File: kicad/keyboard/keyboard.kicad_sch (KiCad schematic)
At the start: 119 parts, among them SW1 MX_SWITCH, SW10 MX_SWITCH, SW11 MX_SWITCH, SW12 MX_SWITCH, SW13 MX_SWITCH, SW14 MX_SWITCH, SW15 MX_SWITCH, SW16 MX_SWITCH, SW17 MX_SWITCH, SW18 MX_SWITCH, SW19 MX_SWITCH, SW2 MX_SWITCH, SW20 MX_SWITCH, SW21 MX_SWITCH, SW22 MX_SWITCH, SW23 MX_SWITCH, SW24 MX_SWITCH, SW25 MX_SWITCH, SW26 MX_SWITCH, SW27 MX_SWITCH, SW28 MX_SWITCH, SW29 MX_SWITCH, SW3 MX_SWITCH, SW30 MX_SWITCH, SW31 MX_SWITCH, SW32 MX_SWITCH, SW33 MX_SWITCH, SW34 MX_SWITCH, SW35 MX_SWITCH, SW36 MX_SWITCH, SW37 MX_SWITCH, SW38 MX_SWITCH, SW39 MX_SWITCH, SW4 MX_SWITCH, SW40 MX_SWITCH, SW41 MX_SWITCH, SW42 MX_SWITCH, SW43 MX_SWITCH, SW44 MX_SWITCH, SW45 MX_SWITCH, SW46 MX_SWITCH, SW47 MX_SWITCH, SW48 MX_SWITCH, SW49 MX_SWITCH, SW5 MX_SWITCH, SW50 MX_SWITCH, SW51 MX_SWITCH, SW52 MX_SWITCH, SW53 MX_SWITCH, SW54 MX_SWITCH, SW55 MX_SWITCH, SW56 MX_SWITCH, SW57 MX_SWITCH, SW58 MX_SWITCH, SW59 MX_SWITCH, SW6 MX_SWITCH, SW7 MX_SWITCH, SW8 MX_SWITCH, SW9 MX_SWITCH

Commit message: PCB design (traces not included)
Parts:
- renumbered D56 to D45, D58 to D46, D45 to D47, D46 to D48, D47 to D49, D48 to D50, D49 to D51, D50 to D52, D51 to D53, D52 to D54, D53 to D55, D54 to D56, D55 to D57, D57 to D58, SW56 to SW45, SW58 to SW46, SW45 to SW47, SW46 to SW48, SW47 to SW49, SW48 to SW50, SW49 to SW51, SW50 to SW52, SW51 to SW53, SW52 to SW54, SW53 to SW55, SW54 to SW56, SW55 to SW57, SW57 to SW58
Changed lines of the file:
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@@
 		(dnp no)
 		(fields_autoplaced yes)
-		(property "Reference" "D47"
+		(property "Reference" "D49"
 			(at 71.12 147.3199 90)
 			(effects
@@
 			(project "keyboard"
 				(path "/61642316-f0b7-413d-bb38-e95d75ab1db2"
-					(reference "D47")
+					(reference "D49")
 					(unit 1)
 				)
@@
 		(dnp no)
 		(fields_autoplaced yes)
-		(property "Reference" "SW47"
+		(property "Reference" "SW49"
 			(at 66.04 134.62 0)
 			(effects
@@
 			(project "keyboard"
 				(path "/61642316-f0b7-413d-bb38-e95d75ab1db2"
-					(reference "SW47")
+					(reference "SW49")
 					(unit 1)
 				)
@@
 		(dnp no)
 		(fields_autoplaced yes)
-		(property "Reference" "SW53"
+		(property "Reference" "SW55"
 			(at 142.24 134.62 0)
 			(effects
@@
 			(project "keyboard"
 				(path "/61642316-f0b7-413d-bb38-e95d75ab1db2"
-					(reference "SW53")
+					(reference "SW55")
 					(unit 1)
 				)
@@
 		(dnp no)
 		(fields_autoplaced yes)
-		(property "Reference" "D48"
+		(property "Reference" "D50"
 			(at 83.82 147.3199 90)
 			(effects
@@
 			(project "keyboard"
 				(path "/61642316-f0b7-413d-bb38-e95d75ab1db2"
-					(reference "D48")
+					(reference "D50")
 					(unit 1)
 				)
@@
 		(dnp no)
 		(fields_autoplaced yes)
-		(property "Reference" "SW50"
+		(property "Reference" "SW52"
 			(at 104.14 134.62 0)
 			(effects
@@
 			(project "keyboard"
 				(path "/61642316-f0b7-413d-bb38-e95d75ab1db2"
-					(reference "SW50")
+					(reference "SW52")
 					(unit 1)
 				)
@@
 		(dnp no)
 		(fields_autoplaced yes)
-		(property "Reference" "SW45"
+		(property "Reference" "SW47"
 			(at 40.64 134.62 0)
 			(effects
@@
 			(project "keyboard"
 				(path "/61642316-f0b7-413d-bb38-e95d75ab1db2"
-					(reference "SW45")
+					(reference "SW47")
 					(unit 1)
 				)
@@
 		(dnp no)
 		(fields_autoplaced yes)
-		(property "Reference" "D52"
+		(property "Reference" "D54"
 			(at 134.62 147.3199 90)
 			(effects
@@
 			(project "keyboard"
 				(path "/61642316-f0b7-413d-bb38-e95d75ab1db2"
-					(reference "D52")
+					(reference "D54")
 					(unit 1)
 				)
@@
 		(dnp no)
 		(fields_autoplaced yes)
-		(property "Reference" "D57"
+		(property "Reference" "D58"
 			(at 185.42 147.3199 90)
 			(effects
@@
 			(project "keyboard"
 				(path "/61642316-f0b7-413d-bb38-e95d75ab1db2"
-					(reference "D57")
+					(reference "D58")
 					(unit 1)
 				)
@@
 		(dnp no)
 		(fields_autoplaced yes)
-		(property "Reference" "D46"
+		(property "Reference" "D48"
 			(at 58.42 147.3199 90)
 			(effects
@@
 			(project "keyboard"
 				(path "/61642316-f0b7-413d-bb38-e95d75ab1db2"
-					(reference "D46")
+					(reference "D48")
 					(unit 1)
 				)
@@
 		(dnp no)
 		(fields_autoplaced yes)
-		(property "Reference" "SW58"
+		(property "Reference" "SW46"
 			(at 193.04 109.22 0)
 			(effects
@@
 			(project "keyboard"
 				(path "/61642316-f0b7-413d-bb38-e95d75ab1db2"
-					(reference "SW58")
+					(reference "SW46")
 					(unit 1)
 				)
@@
 		(dnp no)
 		(fields_autoplaced yes)
-		(property "Reference" "SW49"
+		(property "Reference" "SW51"
 			(at 91.44 134.62 0)
 			(effects
@@
 			(project "keyboard"
 				(path "/61642316-f0b7-413d-bb38-e95d75ab1db2"
-					(reference "SW49")
+					(reference "SW51")
 					(unit 1)
 				)
@@
 		(dnp no)
 		(fields_autoplaced yes)
-		(property "Reference" "D54"
+		(property "Reference" "D56"
 			(at 160.02 147.3199 90)
 			(effects
@@
 			(project "keyboard"
 				(path "/61642316-f0b7-413d-bb38-e95d75ab1db2"
-					(reference "D54")
+					(reference "D56")
 					(unit 1)
 				)
@@
 		(dnp no)
 		(fields_autoplaced yes)
-		(property "Reference" "D51"
+		(property "Reference" "D53"
 			(at 121.92 147.3199 90)
 			(effects
@@
 			(project "keyboard"
 				(path "/61642316-f0b7-413d-bb38-e95d75ab1db2"
-					(reference "D51")
+					(reference "D53")
 					(unit 1)
 				)
@@
 		(dnp no)
 		(fields_autoplaced yes)
-		(property "Reference" "SW56"
+		(property "Reference" "SW45"
 			(at 180.34 109.22 0)
 			(effects
@@
 			(project "keyboard"
 				(path "/61642316-f0b7-413d-bb38-e95d75ab1db2"
-					(reference "SW56")
+					(reference "SW45")
 					(unit 1)
 				)
@@
 		(dnp no)
 		(fields_autoplaced yes)
-		(property "Reference" "D58"
+		(property "Reference" "D46"
 			(at 198.12 121.9199 90)
 			(effects
@@
 			(project "keyboard"
 				(path "/61642316-f0b7-413d-bb38-e95d75ab1db2"
-					(reference "D58")
+					(reference "D46")
 					(unit 1)
 				)
@@
 		(dnp no)
 		(fields_autoplaced yes)
-		(property "Reference" "SW46"
+		(property "Reference" "SW48"
 			(at 53.34 134.62 0)
 			(effects
@@
 			(project "keyboard"
 				(path "/61642316-f0b7-413d-bb38-e95d75ab1db2"
-					(reference "SW46")
+					(reference "SW48")
 					(unit 1)
 				)
@@
 		(dnp no)
 		(fields_autoplaced yes)
-		(property "Reference" "SW54"
+		(property "Reference" "SW56"
 			(at 154.94 134.62 0)
 			(effects
@@
 			(project "keyboard"
 				(path "/61642316-f0b7-413d-bb38-e95d75ab1db2"
-					(reference "SW54")
+					(reference "SW56")
 					(unit 1)
 				)
@@
 		(dnp no)
 		(fields_autoplaced yes)
-		(property "Reference" "D56"
+		(property "Reference" "D45"
 			(at 185.42 121.9199 90)
 			(effects
@@
 			(project "keyboard"
 				(path "/61642316-f0b7-413d-bb38-e95d75ab1db2"
-					(reference "D56")
+					(reference "D45")
 					(unit 1)
 				)
@@
 		(dnp no)
 		(fields_autoplaced yes)
-		(property "Reference" "D55"
+		(property "Reference" "D57"
 			(at 172.72 147.3199 90)
 			(effects
@@
 			(project "keyboard"
 				(path "/61642316-f0b7-413d-bb38-e95d75ab1db2"
-					(reference "D55")
+					(reference "D57")
 					(unit 1)
 				)
@@
 		(dnp no)
 		(fields_autoplaced yes)
-		(property "Reference" "SW55"
+		(property "Reference" "SW57"
 			(at 167.64 134.62 0)
 			(effects
@@
 			(project "keyboard"
 				(path "/61642316-f0b7-413d-bb38-e95d75ab1db2"
-					(reference "SW55")
+					(reference "SW57")
 					(unit 1)
 				)
@@
 		(dnp no)
 		(fields_autoplaced yes)
-		(property "Reference" "D45"
+		(property "Reference" "D47"
 			(at 45.72 147.3199 90)
 			(effects
@@
 			(project "keyboard"
 				(path "/61642316-f0b7-413d-bb38-e95d75ab1db2"
-					(reference "D45")
+					(reference "D47")
 					(unit 1)
 				)
@@
 		(dnp no)
 		(fields_autoplaced yes)
-		(property "Reference" "D49"
+		(property "Reference" "D51"
 			(at 96.52 147.3199 90)
 			(effects
@@
 			(project "keyboard"
 				(path "/61642316-f0b7-413d-bb38-e95d75ab1db2"
-					(reference "D49")
+					(reference "D51")
 					(unit 1)
 				)
@@
 		(dnp no)
 		(fields_autoplaced yes)
-		(property "Reference" "SW48"
+		(property "Reference" "SW50"
 			(at 78.74 134.62 0)
 			(effects
@@
 			(project "keyboard"
 				(path "/61642316-f0b7-413d-bb38-e95d75ab1db2"
-					(reference "SW48")
+					(reference "SW50")
 					(unit 1)
 				)
@@
 		(dnp no)
 		(fields_autoplaced yes)
-		(property "Reference" "SW57"
+		(property "Reference" "SW58"
 			(at 180.34 134.62 0)
 			(effects
@@
 			(project "keyboard"
 				(path "/61642316-f0b7-413d-bb38-e95d75ab1db2"
-					(reference "SW57")
+					(reference "SW58")
 					(unit 1)
 				)
@@
 		(dnp no)
 		(fields_autoplaced yes)
-		(property "Reference" "D50"
+		(property "Reference" "D52"
 			(at 109.22 147.3199 90)
 			(effects
@@
 			(project "keyboard"
 				(path "/61642316-f0b7-413d-bb38-e95d75ab1db2"
-					(reference "D50")
+					(reference "D52")
 					(unit 1)
 				)
@@
 		(dnp no)
 		(fields_autoplaced yes)
-		(property "Reference" "D53"
+		(property "Reference" "D55"
 			(at 147.32 147.3199 90)
 			(effects
@@
 			(project "keyboard"
 				(path "/61642316-f0b7-413d-bb38-e95d75ab1db2"
-					(reference "D53")
+					(reference "D55")
 					(unit 1)
 				)
@@
 		(dnp no)
 		(fields_autoplaced yes)
-		(property "Reference" "SW51"
+		(property "Reference" "SW53"
 			(at 116.84 134.62 0)
 			(effects
@@
 			(project "keyboard"
 				(path "/61642316-f0b7-413d-bb38-e95d75ab1db2"
-					(reference "SW51")
+					(reference "SW53")
 					(unit 1)
 				)
@@
 		(dnp no)
 		(fields_autoplaced yes)
-		(property "Reference" "SW52"
+		(property "Reference" "SW54"
 			(at 129.54 134.62 0)
 			(effects
@@
 			(project "keyboard"
 				(path "/61642316-f0b7-413d-bb38-e95d75ab1db2"
-					(reference "SW52")
+					(reference "SW54")
 					(unit 1)
 				)

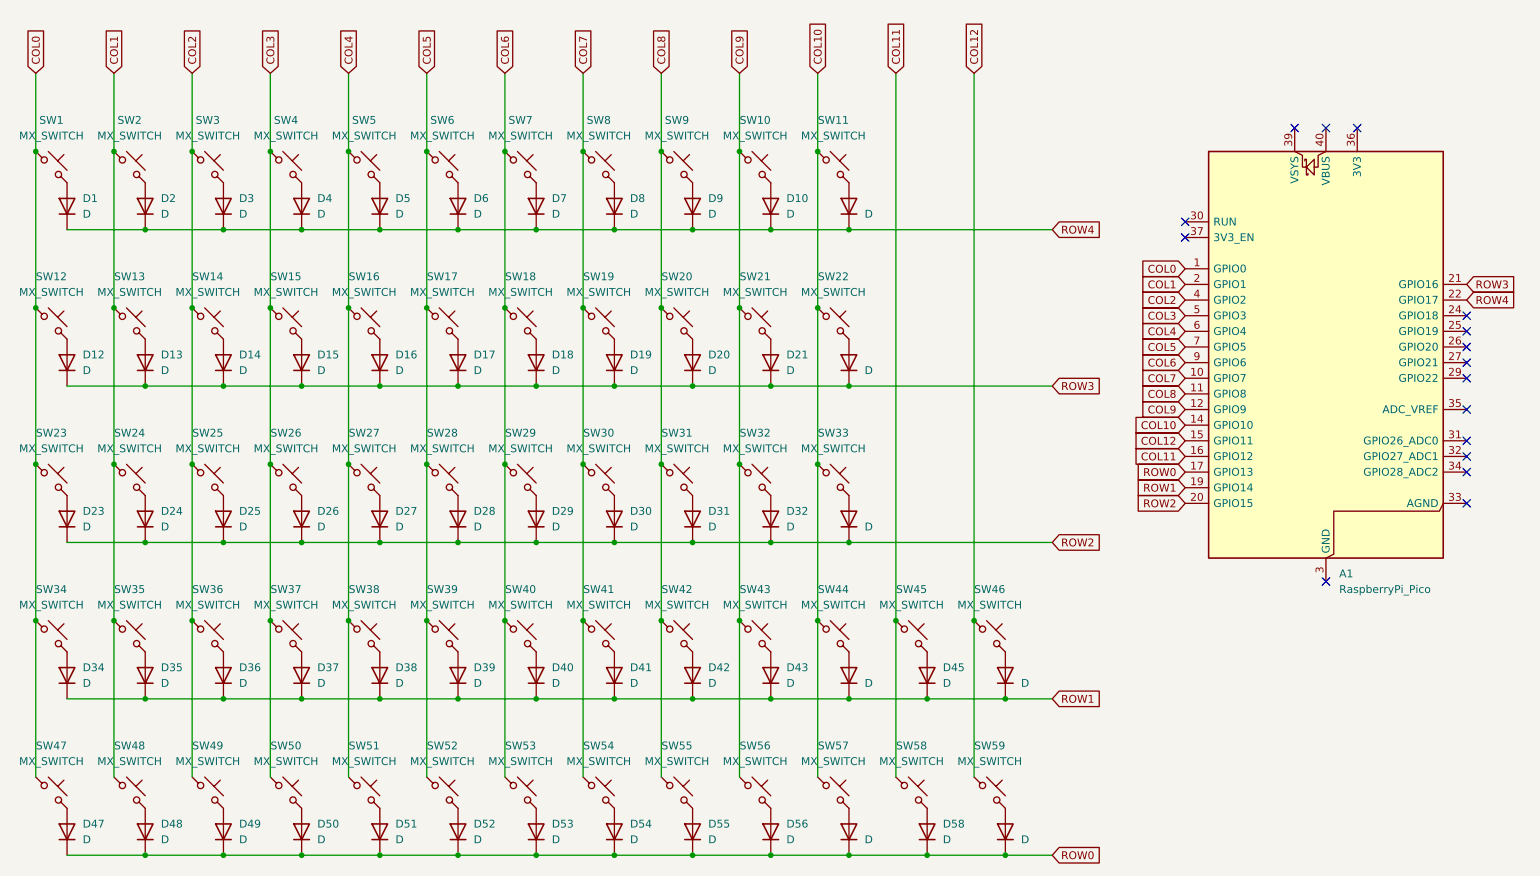
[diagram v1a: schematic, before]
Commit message: Fix incorrect switch positions
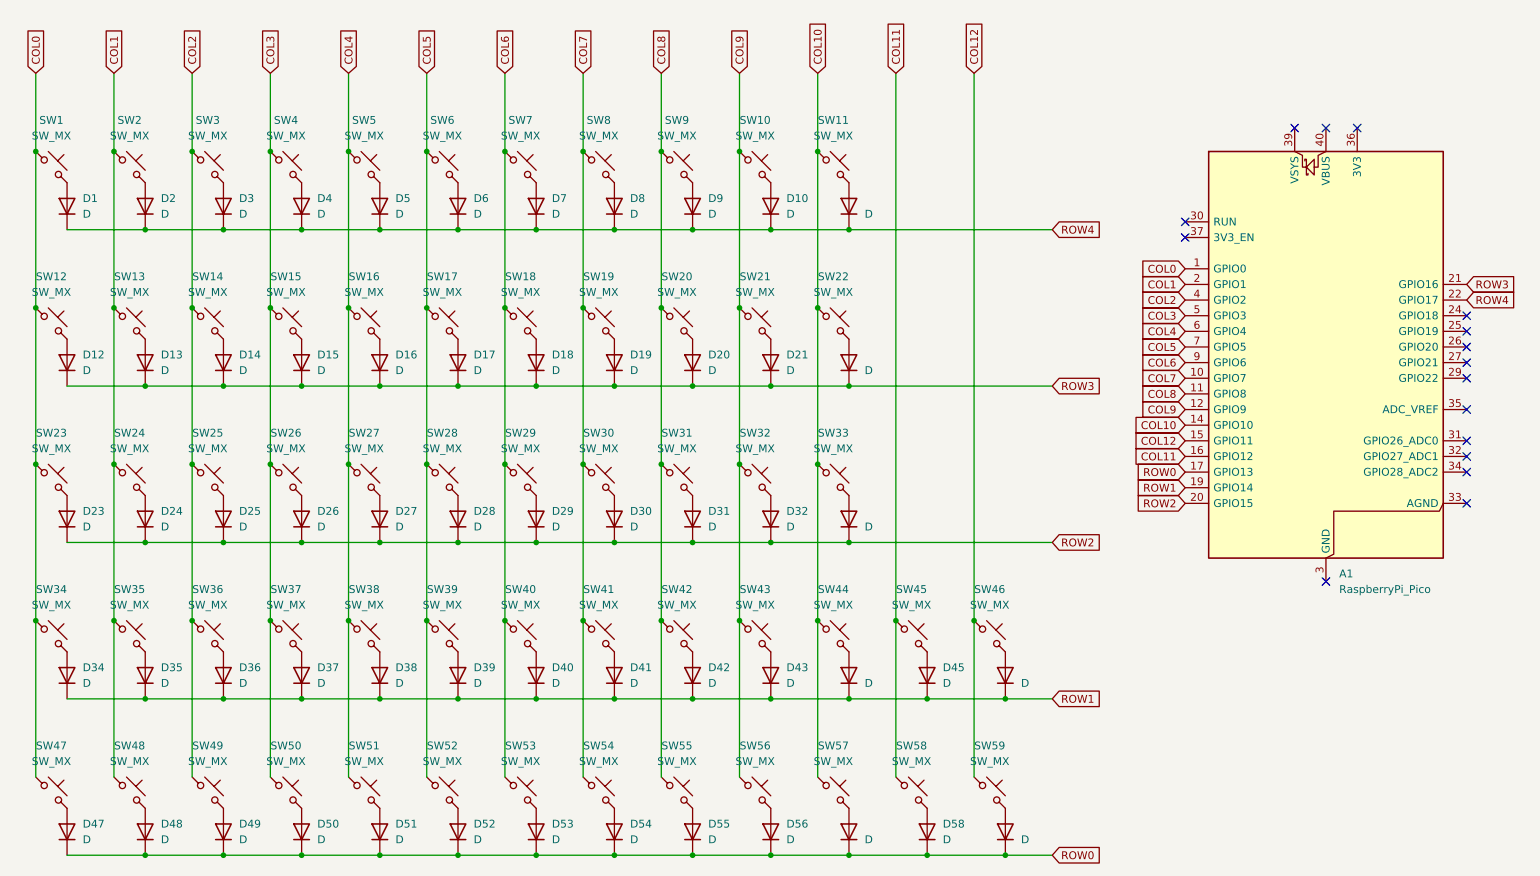
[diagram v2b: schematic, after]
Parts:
- SW1, SW10, SW11, SW12, SW13, SW14, SW15, SW16, SW17, SW18, SW19, SW2, SW20, SW21, SW22, SW23, SW24, SW25, SW26, SW27, SW28, SW29, SW3, SW30, SW31, SW32, SW33, SW34, SW35, SW36, SW37, SW38, SW39, SW4, SW40, SW41, SW42, SW43, SW44, SW45, SW46, SW47, SW48, SW49, SW5, SW50, SW51, SW52, SW53, SW54, SW55, SW56, SW57, SW58, SW59, SW6, SW7, SW8, SW9: value MX_SWITCH -> SW_MX
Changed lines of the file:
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@@
 			)
 		)
-		(property "Value" "MX_SWITCH"
+		(property "Value" "SW_MX"
 			(at 66.04 137.16 0)
 			(effects
@@
 			)
 		)
-		(property "Value" "MX_SWITCH"
+		(property "Value" "SW_MX"
 			(at 129.54 86.36 0)
 			(effects
@@
 			)
 		)
-		(property "Value" "MX_SWITCH"
+		(property "Value" "SW_MX"
 			(at 91.44 60.96 0)
 			(effects
@@
 			)
 		)
-		(property "Value" "MX_SWITCH"
+		(property "Value" "SW_MX"
 			(at 91.44 111.76 0)
 			(effects
@@
 			)
 		)
-		(property "Value" "MX_SWITCH"
+		(property "Value" "SW_MX"
 			(at 154.94 86.36 0)
 			(effects
@@
 			)
 		)
-		(property "Value" "MX_SWITCH"
+		(property "Value" "SW_MX"
 			(at 142.24 137.16 0)
 			(effects
@@
 			)
 		)
-		(property "Value" "MX_SWITCH"
+		(property "Value" "SW_MX"
 			(at 129.54 60.96 0)
 			(effects
@@
 			)
 		)
-		(property "Value" "MX_SWITCH"
+		(property "Value" "SW_MX"
 			(at 53.34 111.76 0)
 			(effects
@@
 			)
 		)
-		(property "Value" "MX_SWITCH"
+		(property "Value" "SW_MX"
 			(at 104.14 137.16 0)
 			(effects
@@
 			)
 		)
-		(property "Value" "MX_SWITCH"
+		(property "Value" "SW_MX"
 			(at 116.84 86.36 0)
 			(effects
@@
 			)
 		)
-		(property "Value" "MX_SWITCH"
+		(property "Value" "SW_MX"
 			(at 154.94 60.96 0)
 			(effects
@@
 			)
 		)
-		(property "Value" "MX_SWITCH"
+		(property "Value" "SW_MX"
 			(at 104.14 35.56 0)
 			(effects
@@
 			)
 		)
-		(property "Value" "MX_SWITCH"
+		(property "Value" "SW_MX"
 			(at 40.64 137.16 0)
 			(effects
@@
 			)
 		)
-		(property "Value" "MX_SWITCH"
+		(property "Value" "SW_MX"
 			(at 142.24 86.36 0)
 			(effects
@@
 			)
 		)
-		(property "Value" "MX_SWITCH"
+		(property "Value" "SW_MX"
 			(at 116.84 35.56 0)
 			(effects
@@
 			)
 		)
-		(property "Value" "MX_SWITCH"
+		(property "Value" "SW_MX"
 			(at 167.64 60.96 0)
 			(effects
@@
 			)
 		)
-		(property "Value" "MX_SWITCH"
+		(property "Value" "SW_MX"
 			(at 66.04 35.56 0)
 			(effects
@@
 			)
 		)
-		(property "Value" "MX_SWITCH"
+		(property "Value" "SW_MX"
 			(at 142.24 35.56 0)
 			(effects
@@
 			)
 		)
-		(property "Value" "MX_SWITCH"
+		(property "Value" "SW_MX"
 			(at 40.64 60.96 0)
 			(effects
@@
 			)
 		)
-		(property "Value" "MX_SWITCH"
+		(property "Value" "SW_MX"
 			(at 78.74 86.36 0)
 			(effects
@@
 			)
 		)
-		(property "Value" "MX_SWITCH"
+		(property "Value" "SW_MX"
 			(at 154.94 35.56 0)
 			(effects
@@
 			)
 		)
-		(property "Value" "MX_SWITCH"
+		(property "Value" "SW_MX"
 			(at 193.04 137.16 0)
 			(effects
@@
 			)
 		)
-		(property "Value" "MX_SWITCH"
+		(property "Value" "SW_MX"
 			(at 53.34 60.96 0)
 			(effects
@@
 			)
 		)
-		(property "Value" "MX_SWITCH"
+		(property "Value" "SW_MX"
 			(at 193.04 111.76 0)
 			(effects
@@
 			)
 		)
-		(property "Value" "MX_SWITCH"
+		(property "Value" "SW_MX"
 			(at 116.84 60.96 0)
 			(effects
@@
 			)
 		)
-		(property "Value" "MX_SWITCH"
+		(property "Value" "SW_MX"
 			(at 66.04 86.36 0)
 			(effects
@@
 			)
 		)
-		(property "Value" "MX_SWITCH"
+		(property "Value" "SW_MX"
 			(at 91.44 137.16 0)
 			(effects
@@
 			)
 		)
-		(property "Value" "MX_SWITCH"
+		(property "Value" "SW_MX"
 			(at 167.64 111.76 0)
 			(effects
@@
 			)
 		)
-		(property "Value" "MX_SWITCH"
+		(property "Value" "SW_MX"
 			(at 142.24 111.76 0)
 			(effects
@@
 			)
 		)
-		(property "Value" "MX_SWITCH"
+		(property "Value" "SW_MX"
 			(at 78.74 60.96 0)
 			(effects
@@
 			)
 		)
-		(property "Value" "MX_SWITCH"
+		(property "Value" "SW_MX"
 			(at 91.44 86.36 0)
 			(effects
@@
 			)
 		)
-		(property "Value" "MX_SWITCH"
+		(property "Value" "SW_MX"
 			(at 104.14 111.76 0)
 			(effects
@@
 			)
 		)
-		(property "Value" "MX_SWITCH"
+		(property "Value" "SW_MX"
 			(at 180.34 111.76 0)
 			(effects
@@
 			)
 		)
-		(property "Value" "MX_SWITCH"
+		(property "Value" "SW_MX"
 			(at 167.64 35.56 0)
 			(effects
@@
 			)
 		)
-		(property "Value" "MX_SWITCH"
+		(property "Value" "SW_MX"
 			(at 53.34 137.16 0)
 			(effects
@@
 			)
 		)
-		(property "Value" "MX_SWITCH"
+		(property "Value" "SW_MX"
 			(at 154.94 137.16 0)
 			(effects
@@
 			)
 		)
-		(property "Value" "MX_SWITCH"
+		(property "Value" "SW_MX"
 			(at 91.44 35.56 0)
 			(effects
@@
 			)
 		)
-		(property "Value" "MX_SWITCH"
+		(property "Value" "SW_MX"
 			(at 154.94 111.76 0)
 			(effects
@@
 			)
 		)
-		(property "Value" "MX_SWITCH"
+		(property "Value" "SW_MX"
 			(at 167.64 137.16 0)
 			(effects
@@
 			)
 		)
-		(property "Value" "MX_SWITCH"
+		(property "Value" "SW_MX"
 			(at 104.14 86.36 0)
 			(effects
@@
 			)
 		)
-		(property "Value" "MX_SWITCH"
+		(property "Value" "SW_MX"
 			(at 116.84 111.76 0)
 			(effects
@@
 			)
 		)
-		(property "Value" "MX_SWITCH"
+		(property "Value" "SW_MX"
 			(at 40.64 86.36 0)
 			(effects
@@
 			)
 		)
-		(property "Value" "MX_SWITCH"
+		(property "Value" "SW_MX"
 			(at 78.74 137.16 0)
 			(effects
@@
 			)
 		)
-		(property "Value" "MX_SWITCH"
+		(property "Value" "SW_MX"
 			(at 66.04 60.96 0)
 			(effects
@@
 			)
 		)
-		(property "Value" "MX_SWITCH"
+		(property "Value" "SW_MX"
 			(at 40.64 35.56 0)
 			(effects
@@
 			)
 		)
-		(property "Value" "MX_SWITCH"
+		(property "Value" "SW_MX"
 			(at 78.74 111.76 0)
 			(effects
@@
 			)
 		)
-		(property "Value" "MX_SWITCH"
+		(property "Value" "SW_MX"
 			(at 78.74 35.56 0)
 			(effects
@@
 			)
 		)
-		(property "Value" "MX_SWITCH"
+		(property "Value" "SW_MX"
 			(at 167.64 86.36 0)
 			(effects
@@
 			)
 		)
-		(property "Value" "MX_SWITCH"
+		(property "Value" "SW_MX"
 			(at 180.34 137.16 0)
 			(effects
@@
 			)
 		)
-		(property "Value" "MX_SWITCH"
+		(property "Value" "SW_MX"
 			(at 104.14 60.96 0)
 			(effects
@@
 			)
 		)
-		(property "Value" "MX_SWITCH"
+		(property "Value" "SW_MX"
 			(at 129.54 35.56 0)
 			(effects
@@
 			)
 		)
-		(property "Value" "MX_SWITCH"
+		(property "Value" "SW_MX"
 			(at 53.34 35.56 0)
 			(effects
@@
 			)
 		)
-		(property "Value" "MX_SWITCH"
+		(property "Value" "SW_MX"
 			(at 116.84 137.16 0)
 			(effects
@@
 			)
 		)
-		(property "Value" "MX_SWITCH"
+		(property "Value" "SW_MX"
 			(at 53.34 86.36 0)
 			(effects
@@
 			)
 		)
-		(property "Value" "MX_SWITCH"
+		(property "Value" "SW_MX"
 			(at 142.24 60.96 0)
 			(effects
@@
 			)
 		)
-		(property "Value" "MX_SWITCH"
+		(property "Value" "SW_MX"
 			(at 129.54 137.16 0)
 			(effects
@@
 			)
 		)
-		(property "Value" "MX_SWITCH"
+		(property "Value" "SW_MX"
 			(at 129.54 111.76 0)
 			(effects
@@
 			)
 		)
-		(property "Value" "MX_SWITCH"
+		(property "Value" "SW_MX"
 			(at 66.04 111.76 0)
 			(effects
@@
 			)
 		)
-		(property "Value" "MX_SWITCH"
+		(property "Value" "SW_MX"
 			(at 40.64 111.76 0)
 			(effects

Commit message: Matrix traces
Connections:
- net COL10: now also A1.16 (GPIO12); no longer A1.14 (GPIO10)
- net COL11: now also A1.24 (GPIO18); no longer A1.16 (GPIO12)
- net COL12: now also A1.25 (GPIO19); no longer A1.15 (GPIO11)
- net COL2: now also A1.5 (GPIO3); no longer A1.4 (GPIO2)
- net COL3: now also A1.6 (GPIO4); no longer A1.5 (GPIO3)
- net COL4: now also A1.7 (GPIO5); no longer A1.6 (GPIO4)
- net COL5: now also A1.9 (GPIO6); no longer A1.7 (GPIO5)
- net COL6: now also A1.10 (GPIO7); no longer A1.9 (GPIO6)
- net COL7: now also A1.12 (GPIO9); no longer A1.10 (GPIO7)
- net COL8: now also A1.14 (GPIO10); no longer A1.11 (GPIO8)
- net COL9: now also A1.15 (GPIO11); no longer A1.12 (GPIO9)
- net ROW0: now also A1.21 (GPIO16); no longer A1.17 (GPIO13)
- net ROW1: now also A1.22 (GPIO17); no longer A1.19 (GPIO14)
- net ROW2: now also A1.19 (GPIO14); no longer A1.20 (GPIO15)
- net ROW3: now also A1.11 (GPIO8); no longer A1.21 (GPIO16)
- net ROW4: now also A1.4 (GPIO2); no longer A1.22 (GPIO17)
